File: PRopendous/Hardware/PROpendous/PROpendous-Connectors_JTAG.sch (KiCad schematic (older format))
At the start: 18 parts, among them IC5 FSUSB20, P1 Serial-JTAG, P2 Expansion, U2 microSD, U3 SD, U4 ARM_JTAG, U5 USB-miniB, U6 USB-A

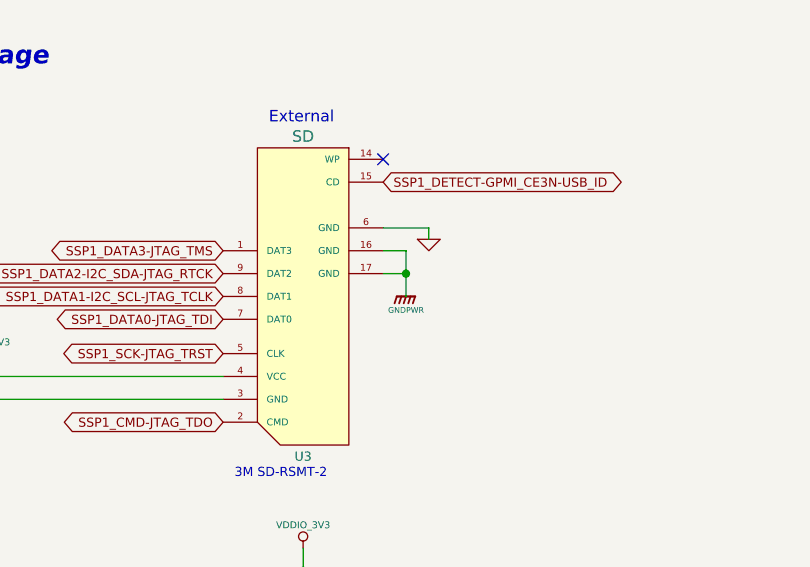
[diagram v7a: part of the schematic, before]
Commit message: First revision of i.MX233-based PROpendous board is complete.
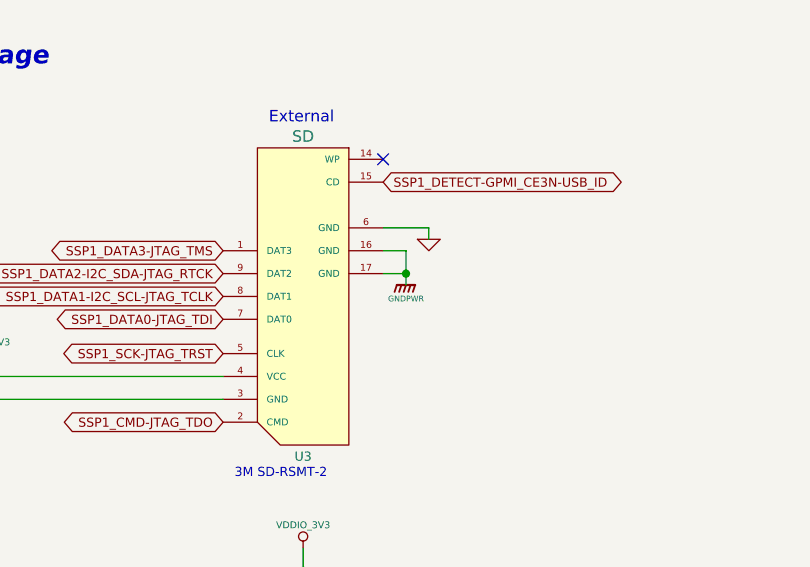
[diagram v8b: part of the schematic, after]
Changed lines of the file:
@@
-EESchema Schematic File Version 2  date 25/04/2010 07:03:32
+EESchema Schematic File Version 2  date 26/04/2010 13:13:01
 LIBS:opendous
 LIBS:device
@@
 Sheet 4 8
 Title "PROpendous"
-Date "25 apr 2010"
+Date "26 apr 2010"
 Rev "1.0"
 Comp "Opendous Inc. (www.opendous.org)"
@@
 Comment4 "www.PROpendous.org"
 $EndDescr
-$Comp
-L CONN_20X2 P2
-U 1 1 4BD415A8
-P 8650 2350
-F 0 "P2" H 8650 3400 60  0000 C CNN
-F 1 "Expansion" V 8650 2350 50  0000 C CNN
-	1    8650 2350
-	1    0    0    -1
-$EndComp
-Text Notes 7100 4700 0    40   ~ 0
-JTAG shares pins with SSP1 so it cannot be used\nat the same time as the external SD card
-$Comp
-L VDDIO_3V3 #PWR031
-U 1 1 4BD246D1
-P 8600 5500
-F 0 "#PWR031" H 8600 5600 30  0001 C CNN
-F 1 "VDDIO_3V3" H 8600 5600 30  0000 C CNN
-	1    8600 5500
-	1    0    0    -1
-$EndComp
-$Comp
-L GND #PWR032
-U 1 1 4BD246D0
-P 8600 5800
-F 0 "#PWR032" H 8600 5800 30  0001 C CNN
-F 1 "GND" H 8600 5730 30  0001 C CNN
-	1    8600 5800
-	1    0    0    -1
-$EndComp
-$Comp
-L C_MINI C77
-U 1 1 4BD246CF
-P 8600 5650
-F 0 "C77" V 8550 5700 30  0000 C CNN
-F 1 "0.1uF" V 8650 5720 25  0000 C CNN
-	1    8600 5650
-	0    1    1    0
-$EndComp
+Connection ~ 5200 1950
+Wire Wire Line
+	5100 1950 5200 1950
 Wire Wire Line
 	8600 5750 8600 5800
@@
 Wire Wire Line
 	5300 1750 5100 1750
-Connection ~ 5200 1950
-Wire Wire Line
-	5200 2050 5200 1850
-Wire Wire Line
-	5200 1850 5100 1850
 Wire Wire Line
 	3100 6850 3100 6800
@@
 Wire Wire Line
 	2250 2100 1200 2100
-Wire Wire Line
-	5100 1950 5200 1950
 Connection ~ 2600 3150
 Wire Wire Line
@@
 	7800 5000 7800 4950
 Connection ~ 7800 5000
+Wire Wire Line
+	5100 1850 5200 1850
+Wire Wire Line
+	5200 1850 5200 2000
+$Comp
+L GNDPWR #PWR031
+U 1 1 4BD5A472
+P 5200 2000
+F 0 "#PWR031" H 5200 2050 40  0001 C CNN
+F 1 "GNDPWR" H 5200 1940 25  0000 C CNN
+	1    5200 2000
+	1    0    0    -1
+$EndComp
+$Comp
+L CONN_20X2 P2
+U 1 1 4BD415A8
+P 8650 2350
+F 0 "P2" H 8650 3400 60  0000 C CNN
+F 1 "Expansion" V 8650 2350 50  0000 C CNN
+	1    8650 2350
+	1    0    0    -1
+$EndComp
+Text Notes 7100 4700 0    40   ~ 0
+JTAG shares pins with SSP1 so it cannot be used\nat the same time as the external SD card
+$Comp
+L VDDIO_3V3 #PWR032
+U 1 1 4BD246D1
+P 8600 5500
+F 0 "#PWR032" H 8600 5600 30  0001 C CNN
+F 1 "VDDIO_3V3" H 8600 5600 30  0000 C CNN
+	1    8600 5500
+	1    0    0    -1
+$EndComp
+$Comp
+L GND #PWR033
+U 1 1 4BD246D0
+P 8600 5800
+F 0 "#PWR033" H 8600 5800 30  0001 C CNN
+F 1 "GND" H 8600 5730 30  0001 C CNN
+	1    8600 5800
+	1    0    0    -1
+$EndComp
+$Comp
+L C_MINI C77
+U 1 1 4BD246CF
+P 8600 5650
+F 0 "C77" V 8550 5700 30  0000 C CNN
+F 1 "0.1uF" V 8650 5720 25  0000 C CNN
+	1    8600 5650
+	0    1    1    0
+$EndComp
 NoConn ~ 7300 6100
 NoConn ~ 7300 6000
@@
 SSP1_DATA1-I2C_SCL-JTAG_TCLK
 $Comp
-L VDDIO_3V3 #PWR033
+L VDDIO_3V3 #PWR034
 U 1 1 4BD232BA
 P 7800 4950
-F 0 "#PWR033" H 7800 5050 30  0001 C CNN
+F 0 "#PWR034" H 7800 5050 30  0001 C CNN
 F 1 "VDDIO_3V3" H 7800 5050 30  0000 C CNN
 	1    7800 4950
@@
 $EndComp
 $Comp
-L GND #PWR034
+L GND #PWR035
 U 1 1 4BD22797
 P 8100 1350
-F 0 "#PWR034" H 8100 1350 30  0001 C CNN
+F 0 "#PWR035" H 8100 1350 30  0001 C CNN
 F 1 "GND" H 8100 1280 30  0001 C CNN
 	1    8100 1350
@@
 $EndComp
 $Comp
-L VDDIO_3V3 #PWR035
+L VDDIO_3V3 #PWR036
 U 1 1 4BD22796
 P 9200 1350
-F 0 "#PWR035" H 9200 1450 30  0001 C CNN
+F 0 "#PWR036" H 9200 1450 30  0001 C CNN
 F 1 "VDDIO_3V3" H 9200 1450 30  0000 C CNN
 	1    9200 1350
@@
 ERC Corrections
 $Comp
-L PWR_FLAG #FLG036
+L PWR_FLAG #FLG037
 U 1 1 4BD12638
 P 10900 900
-F 0 "#FLG036" H 10900 1170 30  0001 C CNN
+F 0 "#FLG037" H 10900 1170 30  0001 C CNN
 F 1 "PWR_FLAG" H 10900 1130 30  0000 C CNN
 	1    10900 900
@@
 $EndComp
 $Comp
-L GND #PWR037
+L GND #PWR038
 U 1 1 4BD0D436
 P 5300 1800
-F 0 "#PWR037" H 5300 1800 30  0001 C CNN
+F 0 "#PWR038" H 5300 1800 30  0001 C CNN
 F 1 "GND" H 5300 1730 30  0001 C CNN
 	1    5300 1800
@@
 $EndComp
 $Comp
-L GND #PWR038
+L GND #PWR039
 U 1 1 4BCED9D8
 P 3100 7100
-F 0 "#PWR038" H 3100 7100 30  0001 C CNN
+F 0 "#PWR039" H 3100 7100 30  0001 C CNN
 F 1 "GND" H 3100 7030 30  0001 C CNN
 	1    3100 7100
@@
 $EndComp
 $Comp
-L VDDIO_3V3 #PWR039
+L VDDIO_3V3 #PWR040
 U 1 1 4BCED9D5
 P 3100 6800
-F 0 "#PWR039" H 3100 6900 30  0001 C CNN
+F 0 "#PWR040" H 3100 6900 30  0001 C CNN
 F 1 "VDDIO_3V3" H 3100 6900 30  0000 C CNN
 	1    3100 6800
@@
 Storage
 $Comp
-L GND_USB-B #PWR040
+L GND_USB-B #PWR041
 U 1 1 4BCE8625
 P 2250 6375
-F 0 "#PWR040" H 2250 6375 30  0001 C CNN
+F 0 "#PWR041" H 2250 6375 30  0001 C CNN
 F 1 "GND_USB-B" H 2250 6305 30  0000 C CNN
 	1    2250 6375
@@
 When PWM2-GPMI_RDY3 enables the\nUSB Host VBUS Generator it will also\nswitch the active USB connector to USB-A
 $Comp
-L GND #PWR041
+L GND #PWR042
 U 1 1 4BCC707A
 P 4200 6050
-F 0 "#PWR041" H 4200 6050 30  0001 C CNN
+F 0 "#PWR042" H 4200 6050 30  0001 C CNN
 F 1 "GND" H 4200 5980 30  0001 C CNN
 	1    4200 6050
@@
 $EndComp
 $Comp
-L VBUS_HOST #PWR042
+L VBUS_HOST #PWR043
 U 1 1 4BCC7077
 P 1950 5450
-F 0 "#PWR042" H 1950 5550 30  0001 C CNN
+F 0 "#PWR043" H 1950 5550 30  0001 C CNN
 F 1 "VBUS_HOST" V 1950 5650 30  0000 C CNN
 	1    1950 5450
@@
 $EndComp
 $Comp
-L VBUS #PWR043
+L VBUS #PWR044
 U 1 1 4BCC5C20
 P 2250 6250
-F 0 "#PWR043" H 2250 6350 30  0001 C CNN
+F 0 "#PWR044" H 2250 6350 30  0001 C CNN
 F 1 "VBUS" V 2250 6400 30  0000 C CNN
 	1    2250 6250
@@
 The FSUSB20 has 7kV of ESD Protection
 $Comp
-L GND #PWR044
+L GND #PWR045
 U 1 1 4BCC5AB5
 P 4000 6050
-F 0 "#PWR044" H 4000 6050 30  0001 C CNN
+F 0 "#PWR045" H 4000 6050 30  0001 C CNN
 F 1 "GND" H 4000 5980 30  0001 C CNN
 	1    4000 6050
@@
 DPa
 $Comp
-L GND #PWR045
+L GND #PWR046
 U 1 1 4BCC59FD
 P 3100 6300
-F 0 "#PWR045" H 3100 6300 30  0001 C CNN
+F 0 "#PWR046" H 3100 6300 30  0001 C CNN
 F 1 "GND" H 3100 6230 30  0001 C CNN
 	1    3100 6300
@@
 $EndComp
 $Comp
-L VDDIO_3V3 #PWR046
+L VDDIO_3V3 #PWR047
 U 1 1 4BCC59F5
 P 3100 5300
-F 0 "#PWR046" H 3100 5400 30  0001 C CNN
+F 0 "#PWR047" H 3100 5400 30  0001 C CNN
 F 1 "VDDIO_3V3" H 3100 5400 30  0000 C CNN
 	1    3100 5300
@@
 $EndComp
 $Comp
-L GNDPWR #PWR047
+L GNDPWR #PWR048
 U 1 1 4BCC5395
 P 2950 2300
-F 0 "#PWR047" H 2950 2350 40  0001 C CNN
+F 0 "#PWR048" H 2950 2350 40  0001 C CNN
 F 1 "GNDPWR" H 2950 2240 25  0000 C CNN
 	1    2950 2300
 	1    0    0    -1
 $EndComp
-$Comp
-L GNDPWR #PWR048
-U 1 1 4BCC5390
-P 5200 2050
-F 0 "#PWR048" H 5200 2100 40  0001 C CNN
-F 1 "GNDPWR" H 5200 1990 25  0000 C CNN
-	1    5200 2050
-	1    0    0    -1
-$EndComp
